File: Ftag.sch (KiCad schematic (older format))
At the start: 24 parts, among them P1 USB_OTG, U1 FT232H, U2 TXB0108, X1 12 MHz

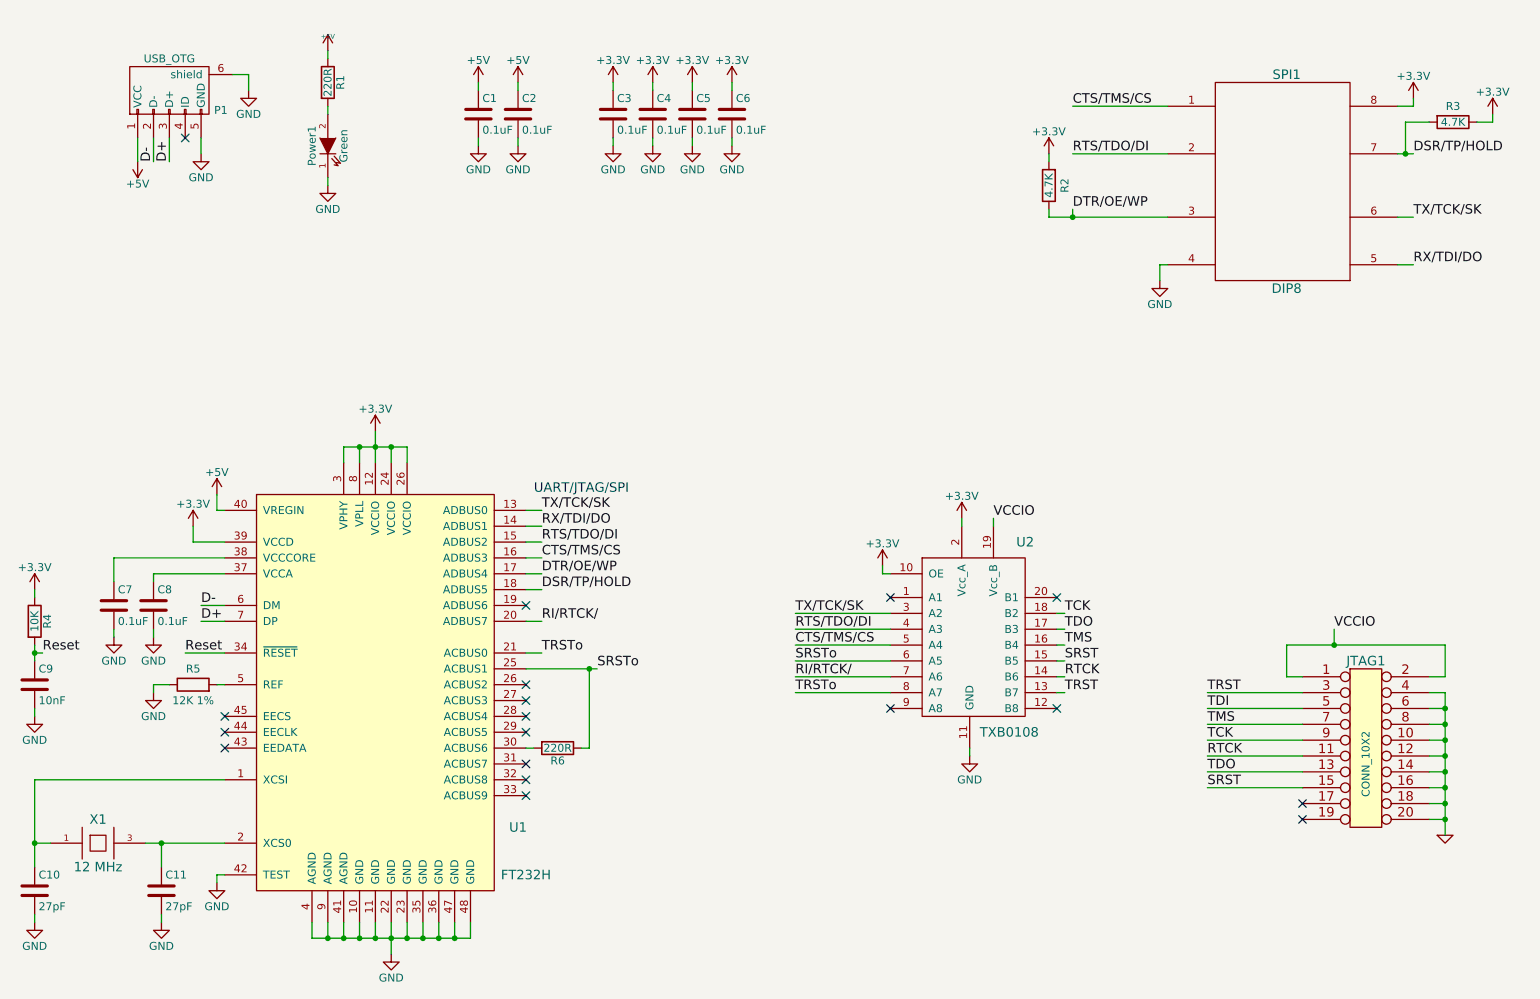
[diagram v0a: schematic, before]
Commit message: Assigned component footprints
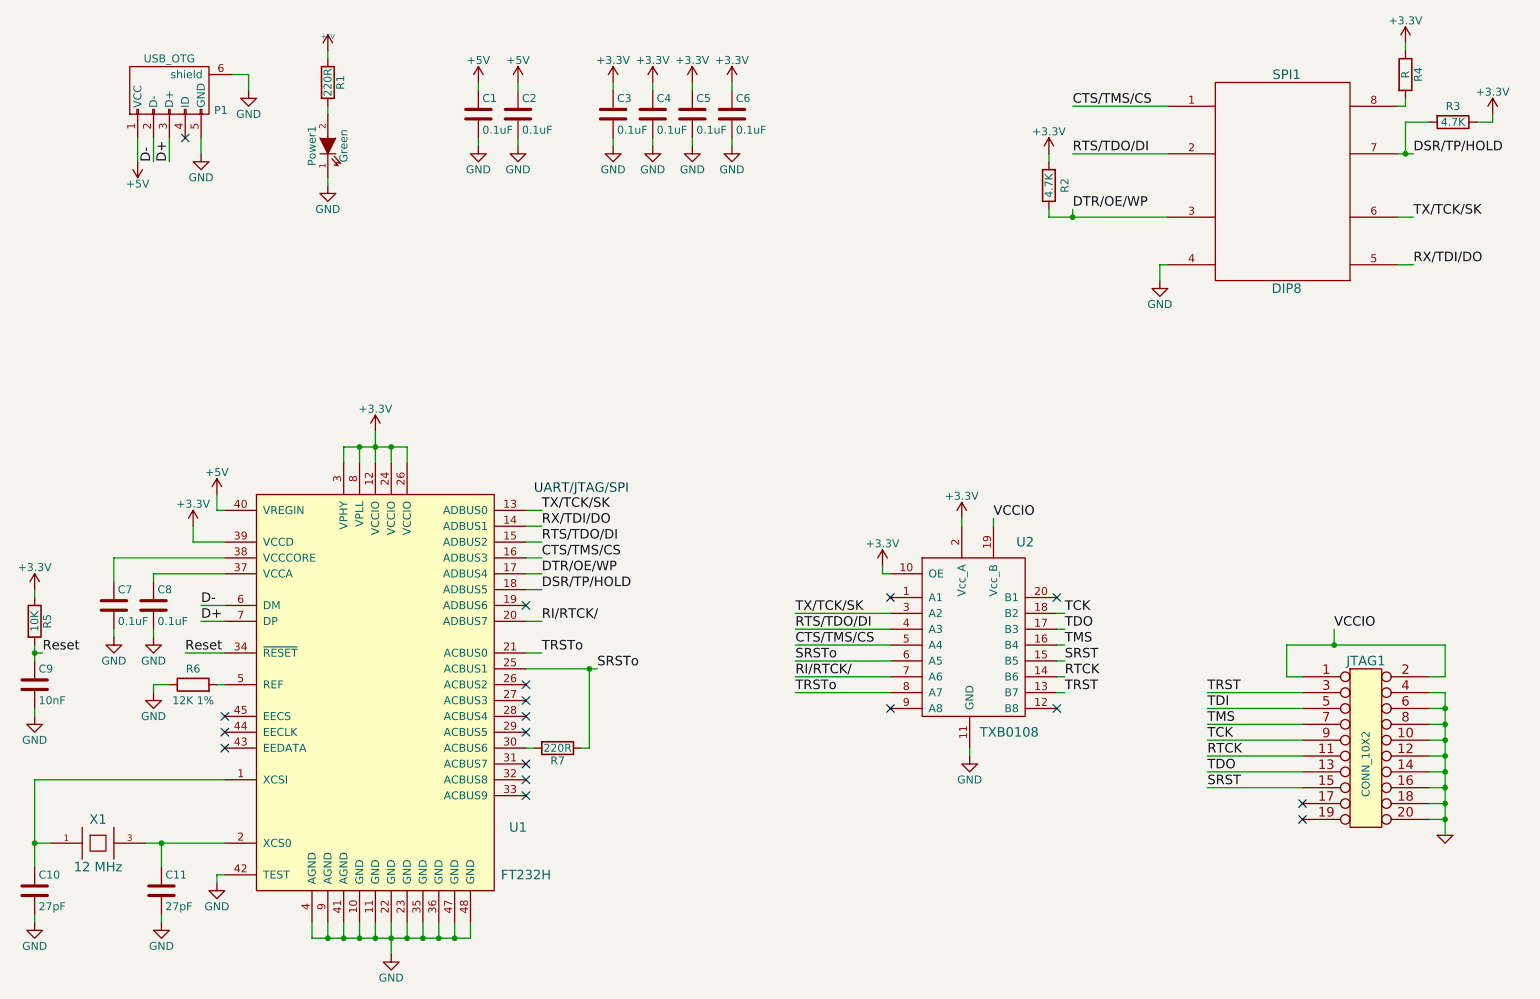
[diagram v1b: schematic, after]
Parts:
- added R4: R, Resistors_SMD:R_0603_HandSoldering, symbol R
- C1, C10, C11, C2, C3, C4, C5, C6, C7, C8, C9: footprint (none) -> Capacitors_SMD:C_0603_HandSoldering
- Power1: footprint (none) -> LEDs:LED_0805
- R1, R2, R3: footprint (none) -> Resistors_SMD:R_0603_HandSoldering
- R5: renamed from R4; footprint (none) -> Resistors_SMD:R_0603_HandSoldering
- R6: renamed from R5; footprint (none) -> Resistors_SMD:R_0603_HandSoldering
- R7: renamed from R6; footprint (none) -> Resistors_SMD:R_0603_HandSoldering
- U1: footprint (none) -> Housings_QFP:LQFP-48_7x7mm_Pitch0.5mm
- U2: footprint (none) -> Housings_SSOP:SSOP-20_4.4x6.5mm_Pitch0.65mm
- X1: footprint (none) -> Crystals:Q_49U3HMS
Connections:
- net +3V3: now also R4.1; no longer SPI1.8
- new net: R4.2, SPI1.8

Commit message: Started board layout
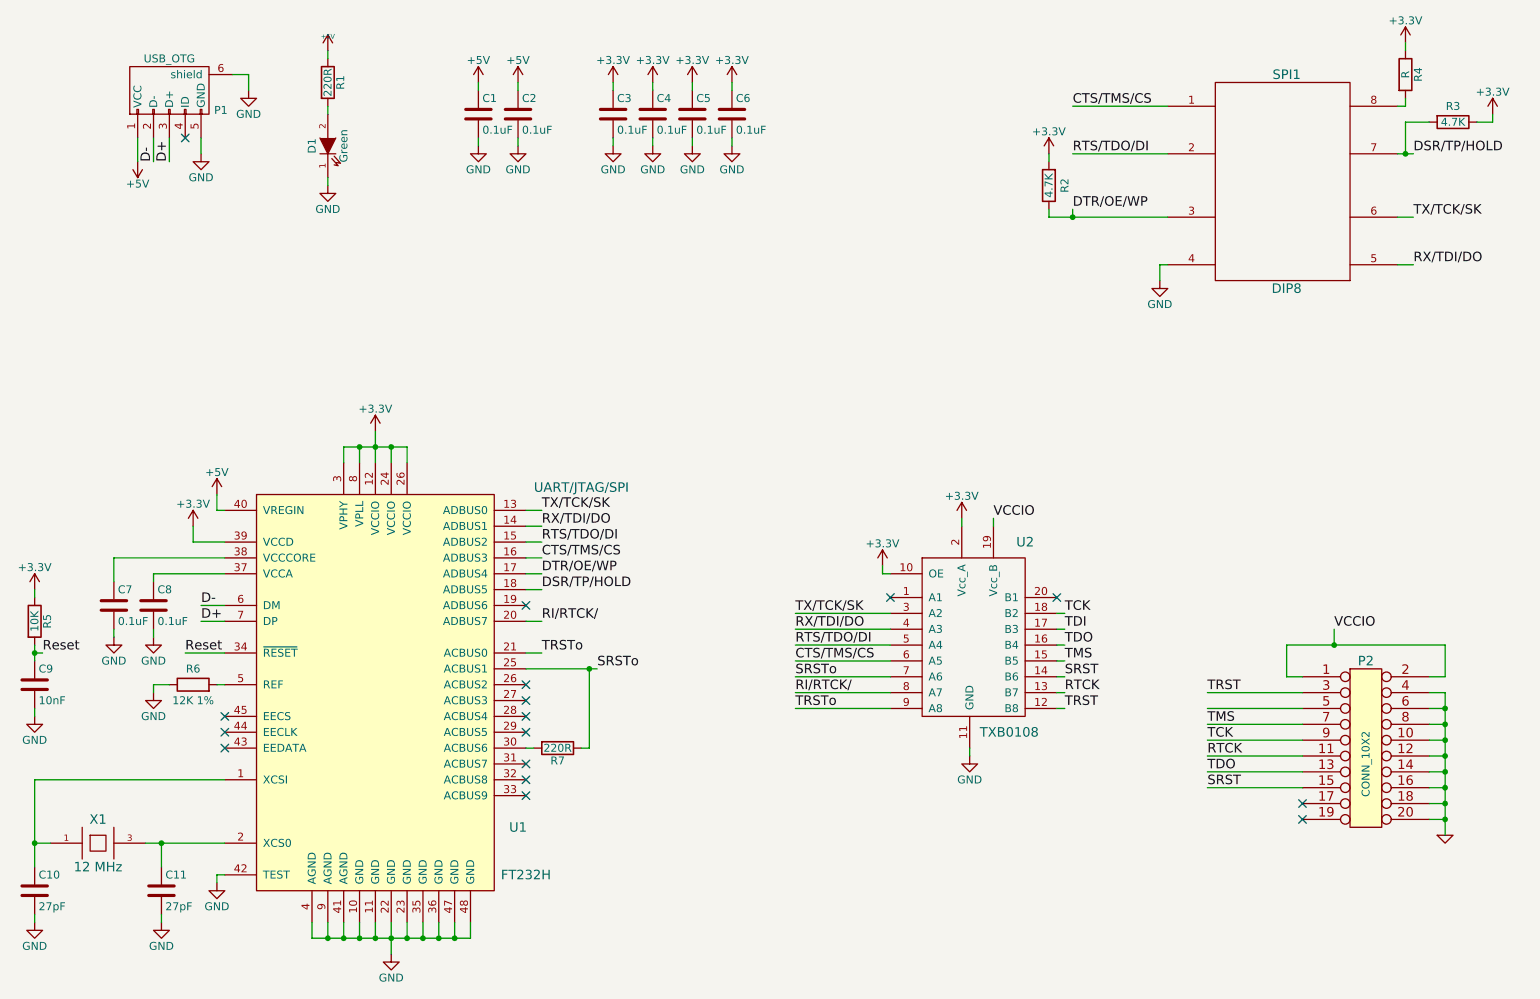
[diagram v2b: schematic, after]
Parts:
- renumbered Power1 to D1, JTAG1 to P2
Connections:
- net CTS/TMS/CS: now also U2.6 (A5); no longer U2.5 (A4)
- net RI/RTCK/: now also U2.8 (A7); no longer U2.7 (A6)
- net RTCK: now also U2.13 (B7); no longer U2.14 (B6)
- net RTS/TDO/DI: now also U2.5 (A4); no longer U2.4 (A3)
- net RX/TDI/DO: now also U2.4 (A3)
- net SRST: now also U2.14 (B6); no longer U2.15 (B5)
- net SRSTo: now also U2.7 (A6); no longer U2.6 (A5)
- net TDI: now also U2.17 (B3); no longer P2.5 (P5)
- net TDO: now also U2.16 (B4); no longer U2.17 (B3)
- net TMS: now also U2.15 (B5); no longer U2.16 (B4)
- net TRST: now also U2.12 (B8); no longer U2.13 (B7)
- net TRSTo: now also U2.9 (A8); no longer U2.8 (A7)
- no-connect marks 18 -> 16
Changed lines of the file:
@@
 Text Label 4350 4100 0    60   ~ 0
 TX/TCK/SK
-Text Label 4350 4200 0    60   ~ 0
+Text Label 5950 4850 0    60   ~ 0
 RX/TDI/DO
 Text Notes 4300 4000 0    60   ~ 0
@@
 TRSTo
 $Comp
-L CONN_10X2 JTAG1
+L CONN_10X2 P2
 U 1 1 53FDF7D1
 P 9550 5600
-F 0 "JTAG1" H 9550 6150 60  0000 C CNN
+F 0 "P2" H 9550 6150 60  0000 C CNN
 F 1 "CONN_10X2" V 9550 5500 50  0000 C CNN
 F 2 "Connect:IDC_Header_Straight_20pins" H 9550 5600 60  0001 C CNN
@@
 NoConn ~ 9150 5950
 NoConn ~ 9150 6050
-Text Label 8550 5350 0    60   ~ 0
+Text Label 7650 4850 0    60   ~ 0
 TDI
 Text Label 8550 5450 0    60   ~ 0
@@
 VCCIO
 $Comp
-L TXB0108 U2
-U 1 1 5758D06F
-P 7500 5400
-F 0 "U2" H 7400 6500 60  0000 C CNN
-F 1 "TXB0108" H 7300 5300 60  0000 C CNN
-F 2 "Housings_SSOP:SSOP-20_4.4x6.5mm_Pitch0.65mm" H 7500 5400 60  0001 C CNN
-F 3 "" H 7500 5400 60  0000 C CNN
-	1    7500 5400
-	1    0    0    -1
-$EndComp
-$Comp
 L GND #PWR05
 U 1 1 5758D11E
@@
 	4600 5600 4650 5600
 Connection ~ 4650 5100
+Text Label 7650 5350 0    60   ~ 0
+TRST
 Text Label 7650 5250 0    60   ~ 0
-TRST
-Text Label 7650 5150 0    60   ~ 0
 RTCK
+Text Label 7650 5050 0    60   ~ 0
+TMS
 Text Label 7650 4950 0    60   ~ 0
-TMS
-Text Label 7650 4850 0    60   ~ 0
 TDO
 Text Label 7650 4750 0    60   ~ 0
 TCK
+Text Label 5950 5250 0    60   ~ 0
+RI/RTCK/
+Text Label 5950 5350 0    60   ~ 0
+TRSTo
 Text Label 5950 5150 0    60   ~ 0
-RI/RTCK/
-Text Label 5950 5250 0    60   ~ 0
-TRSTo
+SRSTo
 Text Label 5950 5050 0    60   ~ 0
-SRSTo
+CTS/TMS/CS
 Text Label 5950 4950 0    60   ~ 0
-CTS/TMS/CS
-Text Label 5950 4850 0    60   ~ 0
 RTS/TDO/DI
 Text Label 5950 4750 0    60   ~ 0
 TX/TCK/SK
-Text Label 7650 5050 0    60   ~ 0
+Text Label 7650 5150 0    60   ~ 0
 SRST
 Wire Wire Line
-	5950 4750 6550 4750
-Wire Wire Line
 	5950 4850 6550 4850
 Wire Wire Line
@@
 	5950 5250 6550 5250
 Wire Wire Line
-	7650 4750 7600 4750
+	5950 5350 6550 5350
 Wire Wire Line
 	7650 4850 7600 4850
 Wire Wire Line
-	7600 4950 7650 4950
-Wire Wire Line
-	7650 5050 7600 5050
-Wire Wire Line
-	7600 5150 7650 5150
-Wire Wire Line
-	7650 5250 7600 5250
+	7650 4950 7600 4950
+Wire Wire Line
+	7600 5050 7650 5050
+Wire Wire Line
+	7650 5150 7600 5150
+Wire Wire Line
+	7600 5250 7650 5250
+Wire Wire Line
+	7650 5350 7600 5350
 NoConn ~ 6550 4650
-NoConn ~ 6550 5350
 NoConn ~ 7600 4650
-NoConn ~ 7600 5350
 $Comp
 L R R1
@@
 $EndComp
 $Comp
-L LED Power1
+L LED D1
 U 1 1 575A35C7
 P 3000 1800
-F 0 "Power1" H 3000 1900 50  0000 C CNN
+F 0 "D1" H 3000 1900 50  0000 C CNN
 F 1 "Green" H 3000 1700 50  0000 C CNN
 F 2 "LEDs:LED_0805" H 3000 1800 50  0001 C CNN
@@
 $EndComp
 $Comp
-L C C2
-U 1 1 575A3CBB
-P 4200 1600
-F 0 "C2" H 4225 1700 50  0000 L CNN
-F 1 "0.1uF" H 4225 1500 50  0000 L CNN
-F 2 "Capacitors_SMD:C_0603_HandSoldering" H 4238 1450 50  0001 C CNN
-F 3 "" H 4200 1600 50  0000 C CNN
-	1    4200 1600
-	1    0    0    -1
-$EndComp
-$Comp
 L C C3
 U 1 1 575A3D00
@@
 $Comp
 L GND #PWR023
-U 1 1 575A4377
-P 4200 1800
-F 0 "#PWR023" H 4200 1550 50  0001 C CNN
-F 1 "GND" H 4200 1650 50  0000 C CNN
-F 2 "" H 4200 1800 50  0000 C CNN
-F 3 "" H 4200 1800 50  0000 C CNN
-	1    4200 1800
-	1    0    0    -1
-$EndComp
-$Comp
-L GND #PWR024
 U 1 1 575A43F0
 P 4800 1800
-F 0 "#PWR024" H 4800 1550 50  0001 C CNN
+F 0 "#PWR023" H 4800 1550 50  0001 C CNN
 F 1 "GND" H 4800 1650 50  0000 C CNN
 F 2 "" H 4800 1800 50  0000 C CNN
@@
 $EndComp
 $Comp
-L GND #PWR025
+L GND #PWR024
 U 1 1 575A4489
 P 5050 1800
-F 0 "#PWR025" H 5050 1550 50  0001 C CNN
+F 0 "#PWR024" H 5050 1550 50  0001 C CNN
 F 1 "GND" H 5050 1650 50  0000 C CNN
 F 2 "" H 5050 1800 50  0000 C CNN
@@
 Wire Wire Line
 	3950 1800 3950 1750
-Wire Wire Line
-	4200 1800 4200 1750
 Wire Wire Line
 	4800 1800 4800 1750
@@
 $EndComp
 $Comp
-L GND #PWR026
+L GND #PWR025
 U 1 1 575A51FC
 P 5300 1800
-F 0 "#PWR026" H 5300 1550 50  0001 C CNN
+F 0 "#PWR025" H 5300 1550 50  0001 C CNN
 F 1 "GND" H 5300 1650 50  0000 C CNN
 F 2 "" H 5300 1800 50  0000 C CNN
@@
 $EndComp
 $Comp
-L GND #PWR027
+L GND #PWR026
 U 1 1 575A524F
 P 5550 1800
-F 0 "#PWR027" H 5550 1550 50  0001 C CNN
+F 0 "#PWR026" H 5550 1550 50  0001 C CNN
 F 1 "GND" H 5550 1650 50  0000 C CNN
 F 2 "" H 5550 1800 50  0000 C CNN
@@
 	5550 1800 5550 1750
 $Comp
-L +5V #PWR028
+L +5V #PWR027
 U 1 1 575A559E
 P 3950 1400
-F 0 "#PWR028" H 3950 1250 50  0001 C CNN
+F 0 "#PWR027" H 3950 1250 50  0001 C CNN
 F 1 "+5V" H 3950 1540 50  0000 C CNN
 F 2 "" H 3950 1400 50  0000 C CNN
@@
 	1    0    0    -1
 $EndComp
-$Comp
-L +5V #PWR029
-U 1 1 575A56D0
-P 4200 1400
-F 0 "#PWR029" H 4200 1250 50  0001 C CNN
-F 1 "+5V" H 4200 1540 50  0000 C CNN
-F 2 "" H 4200 1400 50  0000 C CNN
-F 3 "" H 4200 1400 50  0000 C CNN
-	1    4200 1400
-	1    0    0    -1
-$EndComp
 Wire Wire Line
 	3950 1450 3950 1400
-Wire Wire Line
-	4200 1450 4200 1400
 $Comp
 L C C7
@@
 	1900 4500 1900 4550
 $Comp
-L GND #PWR030
+L GND #PWR028
 U 1 1 575A67D6
 P 1650 4900
-F 0 "#PWR030" H 1650 4650 50  0001 C CNN
+F 0 "#PWR028" H 1650 4650 50  0001 C CNN
 F 1 "GND" H 1650 4750 50  0000 C CNN
 F 2 "" H 1650 4900 50  0000 C CNN
@@
 $EndComp
 $Comp
-L GND #PWR031
+L GND #PWR029
 U 1 1 575A681A
 P 1900 4900
-F 0 "#PWR031" H 1900 4650 50  0001 C CNN
+F 0 "#PWR029" H 1900 4650 50  0001 C CNN
 F 1 "GND" H 1900 4750 50  0000 C CNN
 F 2 "" H 1900 4900 50  0000 C CNN
@@
 $EndComp
 $Comp
-L GND #PWR032
+L GND #PWR030
 U 1 1 575A7A60
 P 1150 5400
-F 0 "#PWR032" H 1150 5150 50  0001 C CNN
+F 0 "#PWR030" H 1150 5150 50  0001 C CNN
 F 1 "GND" H 1150 5250 50  0000 C CNN
 F 2 "" H 1150 5400 50  0000 C CNN
@@
 	1150 5400 1150 5350
 $Comp
-L GND #PWR033
+L GND #PWR031
 U 1 1 575A7E84
 P 1900 5250
-F 0 "#PWR033" H 1900 5000 50  0001 C CNN
+F 0 "#PWR031" H 1900 5000 50  0001 C CNN
 F 1 "GND" H 1900 5100 50  0000 C CNN
 F 2 "" H 1900 5250 50  0000 C CNN
@@
 	1900 5200 2000 5200
 $Comp
-L GND #PWR034
+L GND #PWR032
 U 1 1 575A8639
 P 1150 6700
-F 0 "#PWR034" H 1150 6450 50  0001 C CNN
+F 0 "#PWR032" H 1150 6450 50  0001 C CNN
 F 1 "GND" H 1150 6550 50  0000 C CNN
 F 2 "" H 1150 6700 50  0000 C CNN
@@
 $EndComp
 $Comp
-L GND #PWR035
+L GND #PWR033
 U 1 1 575A8693
 P 1950 6700
-F 0 "#PWR035" H 1950 6450 50  0001 C CNN
+F 0 "#PWR033" H 1950 6450 50  0001 C CNN
 F 1 "GND" H 1950 6550 50  0000 C CNN
 F 2 "" H 1950 6700 50  0000 C CNN
@@
 $EndComp
 $Comp
-L GND #PWR036
+L GND #PWR034
 U 1 1 575A86E6
 P 3400 6900
-F 0 "#PWR036" H 3400 6650 50  0001 C CNN
+F 0 "#PWR034" H 3400 6650 50  0001 C CNN
 F 1 "GND" H 3400 6750 50  0000 C CNN
 F 2 "" H 3400 6900 50  0000 C CNN
@@
 $EndComp
 $Comp
-L GND #PWR037
+L GND #PWR035
 U 1 1 575A9192
 P 2300 6450
-F 0 "#PWR037" H 2300 6200 50  0001 C CNN
+F 0 "#PWR035" H 2300 6200 50  0001 C CNN
 F 1 "GND" H 2300 6300 50  0000 C CNN
 F 2 "" H 2300 6450 50  0000 C CNN
@@
 Wire Wire Line
 	9800 1200 9800 1150
+$Comp
+L TXB0108 U2
+U 1 1 5758D06F
+P 7500 5400
+F 0 "U2" H 7400 6500 60  0000 C CNN
+F 1 "TXB0108" H 7300 5300 60  0000 C CNN
+F 2 "Housings_SSOP:SSOP-20_4.4x6.5mm_Pitch0.65mm" H 7500 5400 60  0001 C CNN
+F 3 "" H 7500 5400 60  0000 C CNN
+	1    7500 5400
+	1    0    0    -1
+$EndComp
+Wire Wire Line
+	5950 4750 6550 4750
+Wire Wire Line
+	7600 4750 7650 4750
+Text Label 4350 4200 0    60   ~ 0
+RX/TDI/DO
+Wire Wire Line
+	4200 1450 4200 1400
+$Comp
+L +5V #PWR036
+U 1 1 575A56D0
+P 4200 1400
+F 0 "#PWR036" H 4200 1250 50  0001 C CNN
+F 1 "+5V" H 4200 1540 50  0000 C CNN
+F 2 "" H 4200 1400 50  0000 C CNN
+F 3 "" H 4200 1400 50  0000 C CNN
+	1    4200 1400
+	1    0    0    -1
+$EndComp
+Wire Wire Line
+	4200 1800 4200 1750
+$Comp
+L GND #PWR037
+U 1 1 575A4377
+P 4200 1800
+F 0 "#PWR037" H 4200 1550 50  0001 C CNN
+F 1 "GND" H 4200 1650 50  0000 C CNN
+F 2 "" H 4200 1800 50  0000 C CNN
+F 3 "" H 4200 1800 50  0000 C CNN
+	1    4200 1800
+	1    0    0    -1
+$EndComp
+$Comp
+L C C2
+U 1 1 575A3CBB
+P 4200 1600
+F 0 "C2" H 4225 1700 50  0000 L CNN
+F 1 "0.1uF" H 4225 1500 50  0000 L CNN
+F 2 "Capacitors_SMD:C_0603_HandSoldering" H 4238 1450 50  0001 C CNN
+F 3 "" H 4200 1600 50  0000 C CNN
+	1    4200 1600
+	1    0    0    -1
+$EndComp
 $EndSCHEMATC

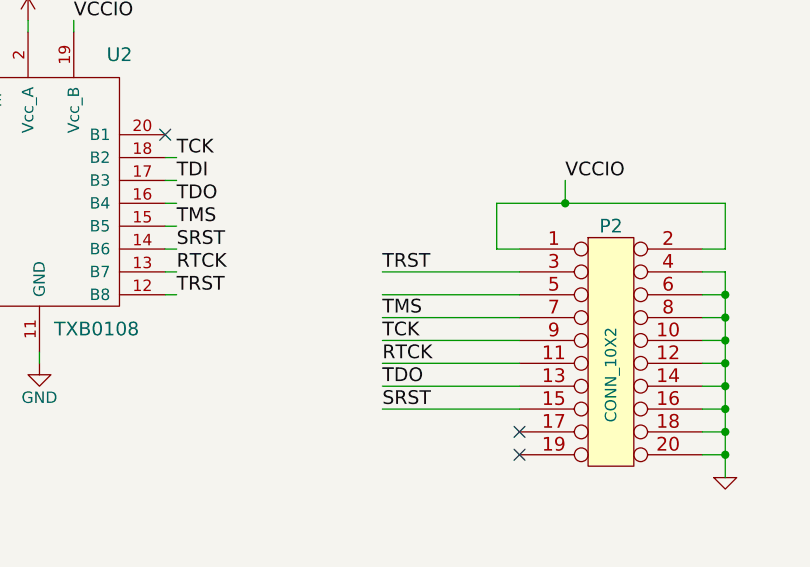
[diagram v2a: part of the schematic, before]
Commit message: Added some routing
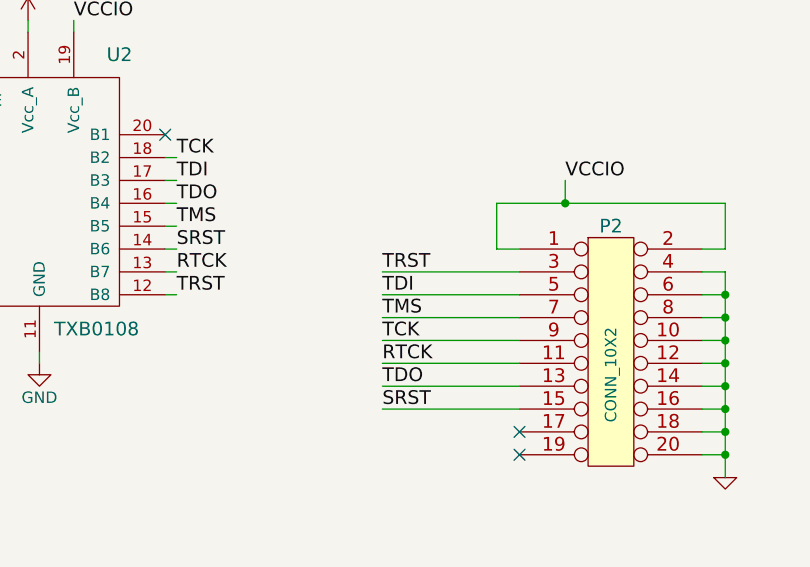
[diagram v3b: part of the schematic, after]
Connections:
- net TDI: now also P2.5 (P5)
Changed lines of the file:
@@
 	1    0    0    -1
 $EndComp
+Text Label 8550 5350 0    60   ~ 0
+TDI
 $EndSCHEMATC
